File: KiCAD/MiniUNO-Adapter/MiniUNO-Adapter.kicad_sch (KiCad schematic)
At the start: 3 parts, among them J1 Conn_01x11, J2 Conn_01x11, J3 Conn_01x07

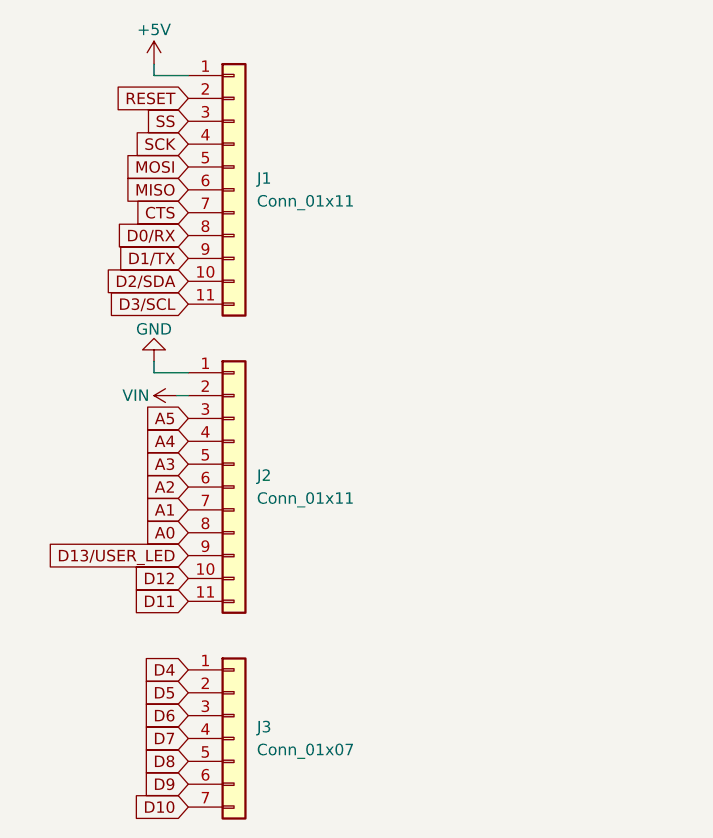
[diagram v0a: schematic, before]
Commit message: Addec pulldown resistors to the VUSB and VIN MOSFETS. Made the adapter PCB
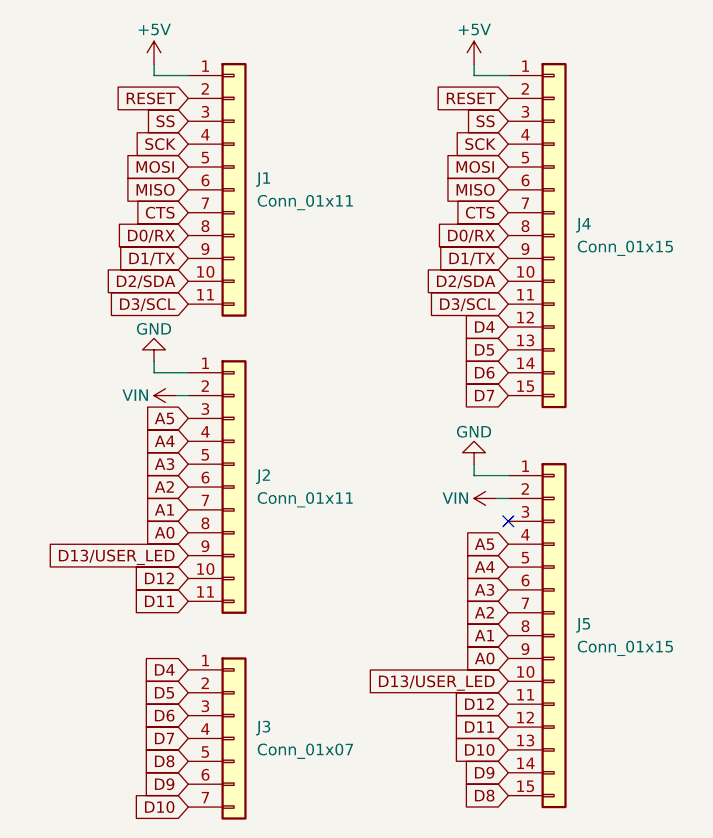
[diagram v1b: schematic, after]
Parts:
- added J4, J5: Conn_01x15, Connector_PinHeader_2.54mm:PinHeader_1x15_P2.54mm_Vertical, symbol Connector_Generic:Conn_01x15
- J1, J2: footprint Connector_PinHeader_2.00mm:PinHeader_1x11_P2.00mm_Vertical -> Connector_PinSocket_2.00mm:PinSocket_1x11_P2.00mm_Vertical
- J3: footprint Connector_PinHeader_2.00mm:PinHeader_1x07_P2.00mm_Vertical -> Connector_PinSocket_2.00mm:PinSocket_1x07_P2.00mm_Vertical
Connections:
- net +5V: now also J4.1 (Pin_1)
- net A0: now also J5.9 (Pin_9)
- net A1: now also J5.8 (Pin_8)
- net A2: now also J5.7 (Pin_7)
- net A3: now also J5.6 (Pin_6)
- net A4: now also J5.5 (Pin_5)
- net A5: now also J5.4 (Pin_4)
- net CTS: now also J4.7 (Pin_7)
- net D0/RX: now also J4.8 (Pin_8)
- net D10: now also J5.13 (Pin_13)
- net D11: now also J5.12 (Pin_12)
- net D12: now also J5.11 (Pin_11)
- net D13/USER_LED: now also J5.10 (Pin_10)
- net D1/TX: now also J4.9 (Pin_9)
- net D2/SDA: now also J4.10 (Pin_10)
- net D3/SCL: now also J4.11 (Pin_11)
- net D4: now also J4.12 (Pin_12)
- net D5: now also J4.13 (Pin_13)
- net D6: now also J4.14 (Pin_14)
- net D7: now also J4.15 (Pin_15)
- net D8: now also J5.15 (Pin_15)
- net D9: now also J5.14 (Pin_14)
- net GND: now also J5.1 (Pin_1)
- net MISO: now also J4.6 (Pin_6)
- net MOSI: now also J4.5 (Pin_5)
- net RESET: now also J4.2 (Pin_2)
- net SCK: now also J4.4 (Pin_4)
- net SS: now also J4.3 (Pin_3)
- net VIN: now also J5.2 (Pin_2)
- no-connect marks 0 -> 1
